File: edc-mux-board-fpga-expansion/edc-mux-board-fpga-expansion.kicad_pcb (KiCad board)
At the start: 4 copper layers, 224.5 x 177.5 mm, 375 parts, among them J1 DC-62F, J2 Device 8, J3 Device 9, J4 Device 10, J5 Device 11, J6 Device 12, J7 Device 13, J8 Device 14, J9 Device 15, U1 EP5358HUI, U10 TLV320AIC3206, U11 FSA2367, U12 P82B96, U13 TLV320AIC3206, U14 FSA2367, U15 P82B96, U16 TLV320AIC3206, U17 FSA2367, U18 P82B96, U19 TLV320AIC3206, U2 R-78B3.3-2.0, U20 FSA2367, U21 P82B96, U22 TLV320AIC3206, U23 FSA2367, U24 P82B96, U25 TLV320AIC3206, U26 FSA2367, U27 CDCLVC1108, U28 TCA9555RTWR, U29 TCA9548A, U3 P82B96, U4 TLV320AIC3206, U5 FSA2367, U6 P82B96, U7 TLV320AIC3206, U8 FSA2367, U9 P82B96

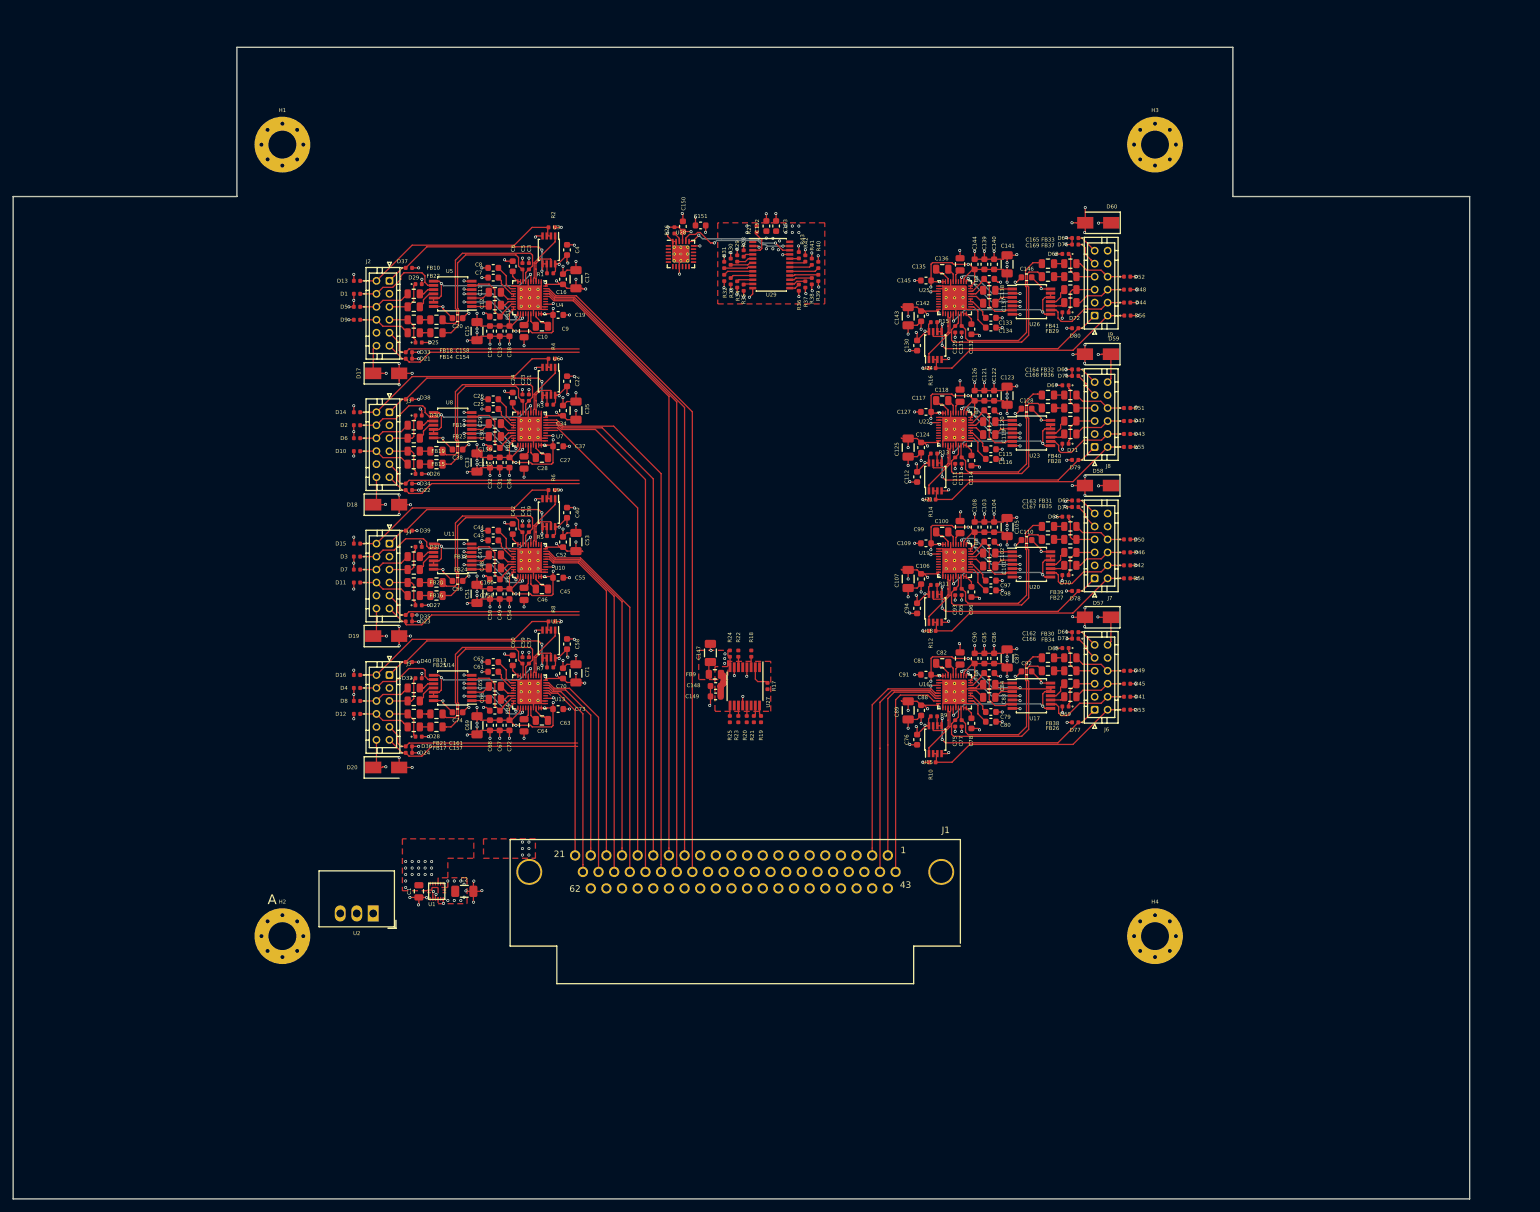
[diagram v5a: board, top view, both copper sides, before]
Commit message: Finished routing of Expansion board. passed DRC
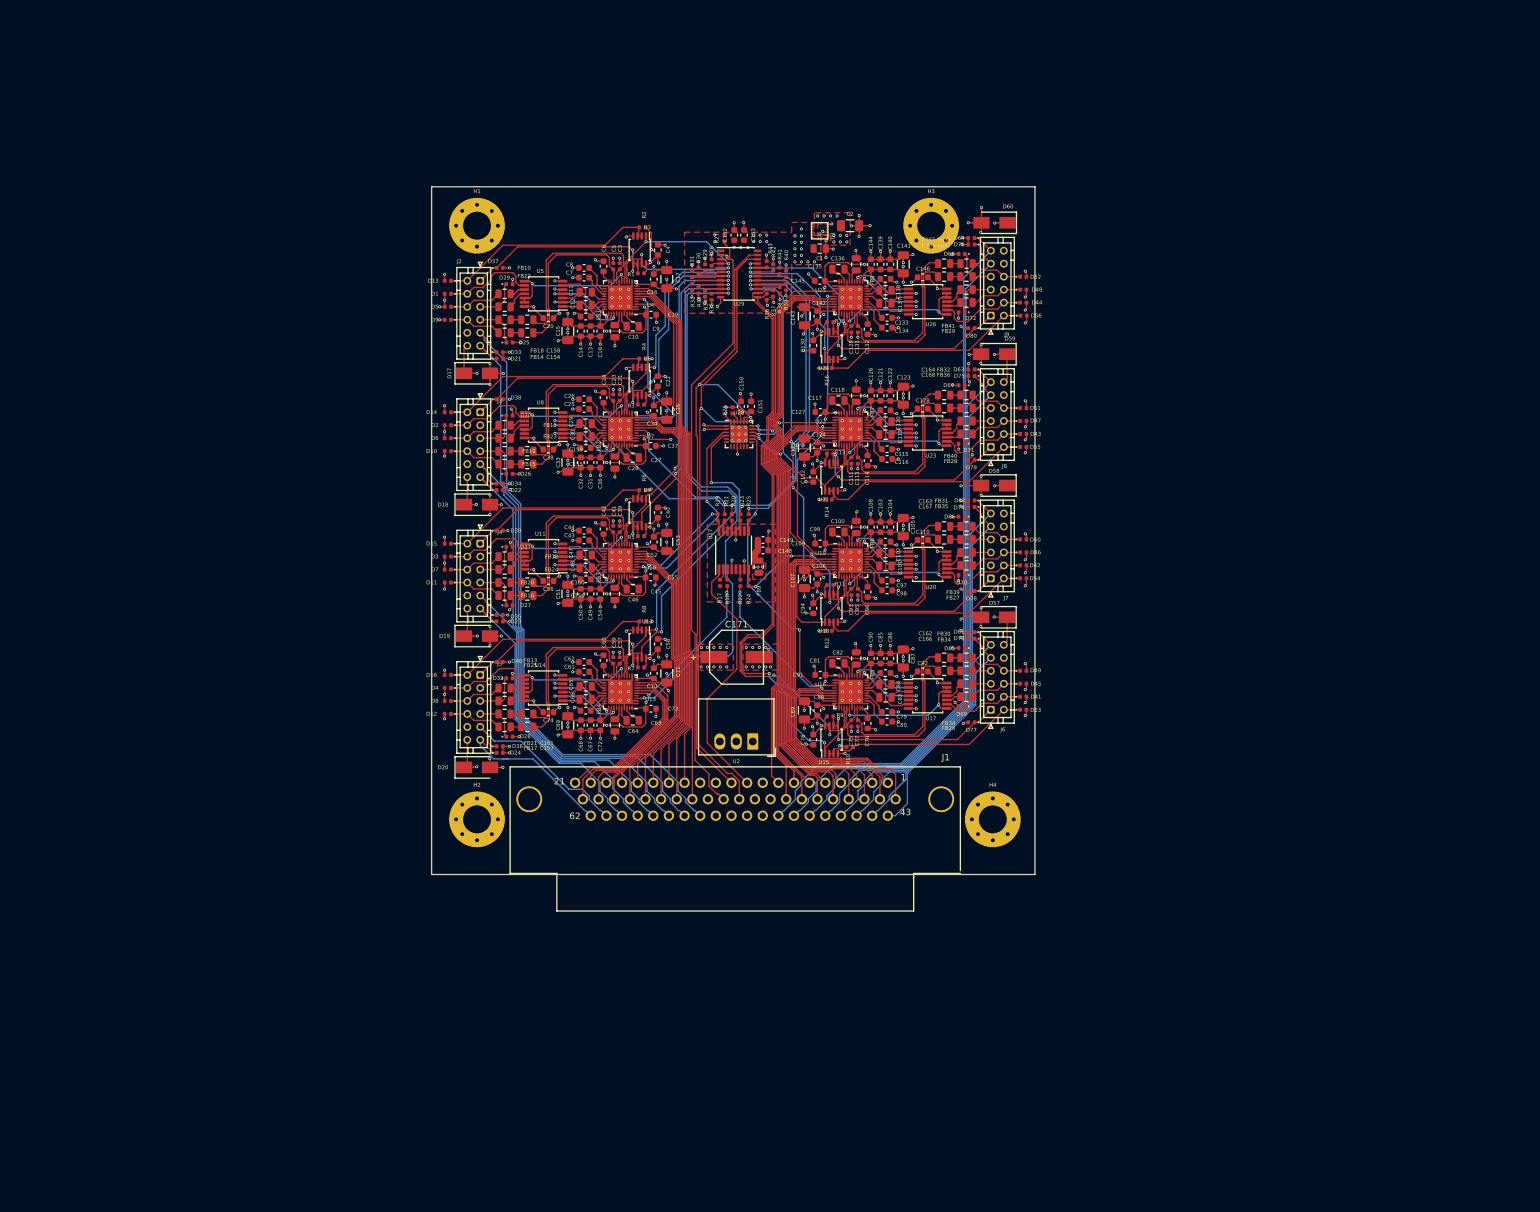
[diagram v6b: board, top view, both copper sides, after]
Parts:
- removed C147: 10uF X7R, Capacitor_SMD:C_1206_3216Metric
- added C171: 47uF, SW-Wurth-Electronics:CP_ELEC_8.3x8.3x11.7mm_SMD, F.Cu at (175.5, 108.5)
- moved C2 118.6 mm to (193.0, 42.0)
- moved U1 117.7 mm to (188.3, 42.8), turned to 180 degrees
- moved C1 116.7 mm to (188.3, 45.5), turned to 0 degrees
- moved U2 64.2 mm to (178.0, 121.5)
- moved H3 36.7 mm to (205.5, 42.0)
- moved H2 35.0 mm to (135.5, 133.5)
- moved H1 32.5 mm to (135.5, 42.0)
- moved R19 31.8 mm to (172.6, 87.0), turned to 270 degrees
- moved R21 31.4 mm to (173.7, 87.0), turned to 270 degrees
- moved R25 31.2 mm to (177.4, 87.0), turned to 270 degrees
- moved R20 31.2 mm to (174.8, 87.0), turned to 270 degrees
- moved R23 31.1 mm to (176.1, 87.0), turned to 270 degrees
- moved H4 30.8 mm to (215.0, 133.5)
- moved C150 29.2 mm to (176.2, 69.9)
- moved U28 29.2 mm to (175.9, 74.1)
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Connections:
- D21 pad 1: /Left Side Connector Interconnects/ID_PIN8 -> /Bottom Side Connector Interconnects/ID_PIN8
- D22 pad 1: /Left Side Connector Interconnects/ID_PIN9 -> /Bottom Side Connector Interconnects/ID_PIN9
- D23 pad 1: /Left Side Connector Interconnects/ID_PIN10 -> /Bottom Side Connector Interconnects/ID_PIN10
- D24 pad 1: /Left Side Connector Interconnects/ID_PIN11 -> /Bottom Side Connector Interconnects/ID_PIN11
- D33 pad 1: /Left Side Connector Interconnects/INT_8 -> /Bottom Side Connector Interconnects/INT_8
- D34 pad 1: /Left Side Connector Interconnects/INT_9 -> /Bottom Side Connector Interconnects/INT_9
- D35 pad 1: /Left Side Connector Interconnects/INT_10 -> /Bottom Side Connector Interconnects/INT_10
- D36 pad 1: /Left Side Connector Interconnects/INT_11 -> /Bottom Side Connector Interconnects/INT_11
- D61 pad 1: /Right Side Connector Interconnects/ID_PIN12 -> /Bottom Side Connector Interconnects/ID_PIN12
- D62 pad 1: /Right Side Connector Interconnects/ID_PIN13 -> /Bottom Side Connector Interconnects/ID_PIN13
- D63 pad 1: /Right Side Connector Interconnects/ID_PIN14 -> /Bottom Side Connector Interconnects/ID_PIN14
- D64 pad 1: /Right Side Connector Interconnects/ID_PIN15 -> /Bottom Side Connector Interconnects/ID_PIN15
- D73 pad 1: /Right Side Connector Interconnects/INT_12 -> /Bottom Side Connector Interconnects/INT_12
- D74 pad 1: /Right Side Connector Interconnects/INT_13 -> /Bottom Side Connector Interconnects/INT_13
- D75 pad 1: /Right Side Connector Interconnects/INT_14 -> /Bottom Side Connector Interconnects/INT_14
- D76 pad 1: /Right Side Connector Interconnects/INT_15 -> /Bottom Side Connector Interconnects/INT_15
- J1 pad 10: (no net) -> CLK2_CODEC
- J1 pad 11: (no net) -> /SDA
- J1 pad 12: (no net) -> +12V
- J1 pad 13: (no net) -> +12V
- J1 pad 30: (no net) -> +12V
- J1 pad 31: (no net) -> +12V
- J1 pad 32: (no net) -> /SCL
- J1 pad 33: (no net) -> /~RESET~I2C
- J1 pad 34: (no net) -> +12V
- J1 pad 43: (no net) -> /Bottom Side Connector Interconnects/INT_12
- J1 pad 44: (no net) -> /Bottom Side Connector Interconnects/ID_PIN12
- J1 pad 45: (no net) -> /Bottom Side Connector Interconnects/INT_13
- J1 pad 46: (no net) -> /Bottom Side Connector Interconnects/ID_PIN13
- J1 pad 47: (no net) -> /Bottom Side Connector Interconnects/INT_14
- J1 pad 48: (no net) -> /Bottom Side Connector Interconnects/ID_PIN14
- J1 pad 49: (no net) -> /Bottom Side Connector Interconnects/INT_15
- J1 pad 50: (no net) -> /Bottom Side Connector Interconnects/ID_PIN15
- J1 pad 51: (no net) -> GND
- J1 pad 52: (no net) -> GND
- J1 pad 53: (no net) -> GND
- J1 pad 54: (no net) -> GND
- J1 pad 55: (no net) -> /Bottom Side Connector Interconnects/INT_8
- J1 pad 56: (no net) -> /Bottom Side Connector Interconnects/ID_PIN8
- J1 pad 57: (no net) -> /Bottom Side Connector Interconnects/INT_9
- J1 pad 58: (no net) -> /Bottom Side Connector Interconnects/ID_PIN9
- J1 pad 59: (no net) -> /Bottom Side Connector Interconnects/INT_10
- J1 pad 60: (no net) -> /Bottom Side Connector Interconnects/ID_PIN10
- J1 pad 61: (no net) -> /Bottom Side Connector Interconnects/INT_11
- J1 pad 62: (no net) -> /Bottom Side Connector Interconnects/ID_PIN11
- J1 pad 9: (no net) -> +12V
- J2 pad 11: /Left Side Connector Interconnects/ID_PIN8 -> /Bottom Side Connector Interconnects/ID_PIN8
- J2 pad 9: /Left Side Connector Interconnects/INT_8 -> /Bottom Side Connector Interconnects/INT_8
- J3 pad 11: /Left Side Connector Interconnects/ID_PIN9 -> /Bottom Side Connector Interconnects/ID_PIN9
- J3 pad 9: /Left Side Connector Interconnects/INT_9 -> /Bottom Side Connector Interconnects/INT_9
- J4 pad 11: /Left Side Connector Interconnects/ID_PIN10 -> /Bottom Side Connector Interconnects/ID_PIN10
- J4 pad 9: /Left Side Connector Interconnects/INT_10 -> /Bottom Side Connector Interconnects/INT_10
- J5 pad 11: /Left Side Connector Interconnects/ID_PIN11 -> /Bottom Side Connector Interconnects/ID_PIN11
- J5 pad 9: /Left Side Connector Interconnects/INT_11 -> /Bottom Side Connector Interconnects/INT_11
- J6 pad 11: /Right Side Connector Interconnects/ID_PIN12 -> /Bottom Side Connector Interconnects/ID_PIN12
- J6 pad 9: /Right Side Connector Interconnects/INT_12 -> /Bottom Side Connector Interconnects/INT_12
- J7 pad 11: /Right Side Connector Interconnects/ID_PIN13 -> /Bottom Side Connector Interconnects/ID_PIN13
- J7 pad 9: /Right Side Connector Interconnects/INT_13 -> /Bottom Side Connector Interconnects/INT_13
- J8 pad 11: /Right Side Connector Interconnects/ID_PIN14 -> /Bottom Side Connector Interconnects/ID_PIN14
- J8 pad 9: /Right Side Connector Interconnects/INT_14 -> /Bottom Side Connector Interconnects/INT_14
- J9 pad 11: /Right Side Connector Interconnects/ID_PIN15 -> /Bottom Side Connector Interconnects/ID_PIN15
- J9 pad 9: /Right Side Connector Interconnects/INT_15 -> /Bottom Side Connector Interconnects/INT_15
- R18 pad 1: /CODEC interconnection sheet/MCLK8 -> /CODEC interconnection sheet/MCLK11
- R19 pad 1: /CODEC interconnection sheet/MCLK15 -> /CODEC interconnection sheet/MCLK10
- R20 pad 1: /CODEC interconnection sheet/MCLK13 -> /CODEC interconnection sheet/MCLK8
- R21 pad 1: /CODEC interconnection sheet/MCLK14 -> /CODEC interconnection sheet/MCLK9
- R22 pad 1: /CODEC interconnection sheet/MCLK9 -> /CODEC interconnection sheet/MCLK12
- R23 pad 1: /CODEC interconnection sheet/MCLK12 -> /CODEC interconnection sheet/MCLK15
- R24 pad 1: /CODEC interconnection sheet/MCLK10 -> /CODEC interconnection sheet/MCLK13
- R25 pad 1: /CODEC interconnection sheet/MCLK11 -> /CODEC interconnection sheet/MCLK14
- U27 pad 1: (no net) -> CLK2_CODEC
- U28 pad 1: (no net) -> /CODEC interconnection sheet/~RESET~8
- U28 pad 10: /CODEC interconnection sheet/~RESET~8 -> (no net)
- U28 pad 11: /CODEC interconnection sheet/~RESET~9 -> (no net)
- U28 pad 12: /CODEC interconnection sheet/~RESET~10 -> (no net)
- U28 pad 13: /CODEC interconnection sheet/~RESET~11 -> (no net)
- U28 pad 2: (no net) -> /CODEC interconnection sheet/~RESET~9
- U28 pad 3: (no net) -> /CODEC interconnection sheet/~RESET~10
- U28 pad 4: (no net) -> /CODEC interconnection sheet/~RESET~11
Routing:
- net /Bottom Side Connector Interconnects/ID_PIN15: track 0.00 -> 111.4 mm
- net /Bottom Side Connector Interconnects/INT_15: track 0.00 -> 108.2 mm
- net /Bottom Side Connector Interconnects/INT_8: track 0.00 -> 101.0 mm
- net /Bottom Side Connector Interconnects/ID_PIN8: track 0.00 -> 95.6 mm
- net /~RESET~I2C: track 4.12 -> 94.0 mm
- net /Bottom Side Connector Interconnects/DOUT15: track 0.00 -> 88.4 mm
- net /Bottom Side Connector Interconnects/WCLK15: track 0.00 -> 88.4 mm
- net /Bottom Side Connector Interconnects/ID_PIN14: track 0.00 -> 86.8 mm
- net /Bottom Side Connector Interconnects/DIN15: track 0.00 -> 85.9 mm
- net /Bottom Side Connector Interconnects/BCLK15: track 0.00 -> 85.8 mm
- net /CODEC interconnection sheet/SCL12: track 8.69 -> 93.7 mm, vias 0 -> 2
- net /CODEC interconnection sheet/SDA12: track 10.1 -> 94.9 mm, vias 0 -> 2
- net /Bottom Side Connector Interconnects/INT_14: track 0.00 -> 83.3 mm
- net /SCL: track 16.9 -> 100.0 mm
- net /SDA: track 18.1 -> 100.0 mm
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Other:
- board size 224.5 x 177.5 mm -> 93 x 106 mm
- board text removed: "A"
